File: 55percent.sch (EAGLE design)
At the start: 141 parts, among them J1 USB4085-GF-A_REVA, U1 ATMEGA32A-PU

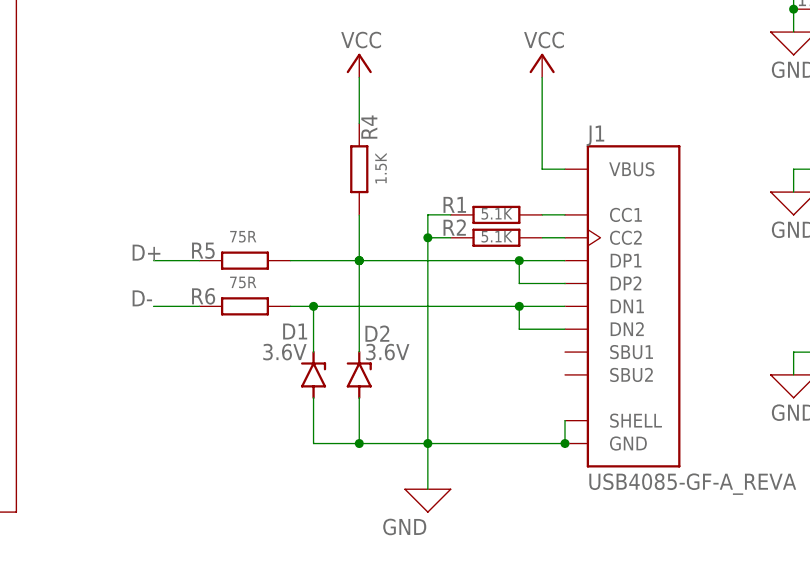
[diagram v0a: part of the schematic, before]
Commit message: Fixed Resistor Placement
If you have used a prior version of any of these files, contact me
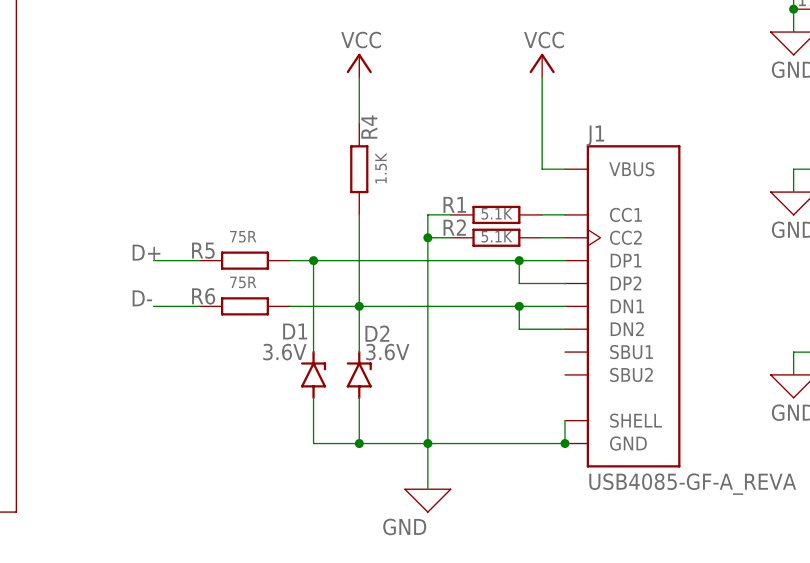
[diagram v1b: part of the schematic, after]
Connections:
- net N$3: now also D1.C; no longer D2.C, R4.2
- net N$7: now also D2.C, R4.2; no longer D1.C
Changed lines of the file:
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@@
 <setting verticaltext="up"/>
 </settings>
-<grid distance="0.1" unitdist="inch" unit="inch" style="lines" multiple="1" display="yes" altdistance="0.01" altunitdist="inch" altunit="inch"/>
+<grid distance="0.1" unitdist="inch" unit="inch" style="lines" multiple="1" display="no" altdistance="0.01" altunitdist="inch" altunit="inch"/>
 <layers>
 <layer number="1" name="Top" color="4" fill="1" visible="no" active="no"/>
@@
 <pinref part="J1" gate="G$1" pin="DP1"/>
 <wire x1="43.18" y1="-2.54" x2="38.1" y2="-2.54" width="0.1524" layer="91"/>
-<pinref part="R4" gate="G$1" pin="2"/>
-<wire x1="38.1" y1="-2.54" x2="20.32" y2="-2.54" width="0.1524" layer="91"/>
-<wire x1="20.32" y1="2.54" x2="20.32" y2="-2.54" width="0.1524" layer="91"/>
-<junction x="20.32" y="-2.54"/>
-<pinref part="D2" gate="1" pin="C"/>
-<wire x1="20.32" y1="-12.7" x2="20.32" y2="-2.54" width="0.1524" layer="91"/>
-<wire x1="12.7" y1="-2.54" x2="20.32" y2="-2.54" width="0.1524" layer="91"/>
-<junction x="20.32" y="-2.54"/>
+<wire x1="38.1" y1="-2.54" x2="15.24" y2="-2.54" width="0.1524" layer="91"/>
 <pinref part="R5" gate="G$1" pin="2"/>
 <pinref part="J1" gate="G$1" pin="DP2"/>
+<wire x1="15.24" y1="-2.54" x2="12.7" y2="-2.54" width="0.1524" layer="91"/>
 <wire x1="43.18" y1="-5.08" x2="38.1" y2="-5.08" width="0.1524" layer="91"/>
 <wire x1="38.1" y1="-5.08" x2="38.1" y2="-2.54" width="0.1524" layer="91"/>
 <junction x="38.1" y="-2.54"/>
+<pinref part="D1" gate="1" pin="C"/>
+<wire x1="15.24" y1="-12.7" x2="15.24" y2="-2.54" width="0.1524" layer="91"/>
+<junction x="15.24" y="-2.54"/>
 </segment>
 </net>
@@
 <wire x1="43.18" y1="-10.16" x2="38.1" y2="-10.16" width="0.1524" layer="91"/>
 <pinref part="J1" gate="G$1" pin="DN1"/>
-<wire x1="15.24" y1="-12.7" x2="15.24" y2="-7.62" width="0.1524" layer="91"/>
-<wire x1="15.24" y1="-7.62" x2="12.7" y2="-7.62" width="0.1524" layer="91"/>
 <pinref part="R6" gate="G$1" pin="2"/>
 <wire x1="43.18" y1="-7.62" x2="38.1" y2="-7.62" width="0.1524" layer="91"/>
-<junction x="15.24" y="-7.62"/>
-<wire x1="38.1" y1="-7.62" x2="15.24" y2="-7.62" width="0.1524" layer="91"/>
+<wire x1="38.1" y1="-7.62" x2="20.32" y2="-7.62" width="0.1524" layer="91"/>
+<wire x1="20.32" y1="-7.62" x2="12.7" y2="-7.62" width="0.1524" layer="91"/>
 <wire x1="38.1" y1="-10.16" x2="38.1" y2="-7.62" width="0.1524" layer="91"/>
 <junction x="38.1" y="-7.62"/>
-<pinref part="D1" gate="1" pin="C"/>
-</segment>
-</net>
+<pinref part="R4" gate="G$1" pin="2"/>
+<pinref part="D2" gate="1" pin="C"/>
+<wire x1="20.32" y1="-12.7" x2="20.32" y2="-7.62" width="0.1524" layer="91"/>
+<junction x="20.32" y="-7.62"/>
+<wire x1="20.32" y1="-7.62" x2="20.32" y2="2.54" width="0.1524" layer="91"/>
+</segment>
+</net>
